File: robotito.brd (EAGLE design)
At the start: 76.2 x 85.1 mm, 44 parts, among them IC1 7805T, IC2 L298, IC3 L298

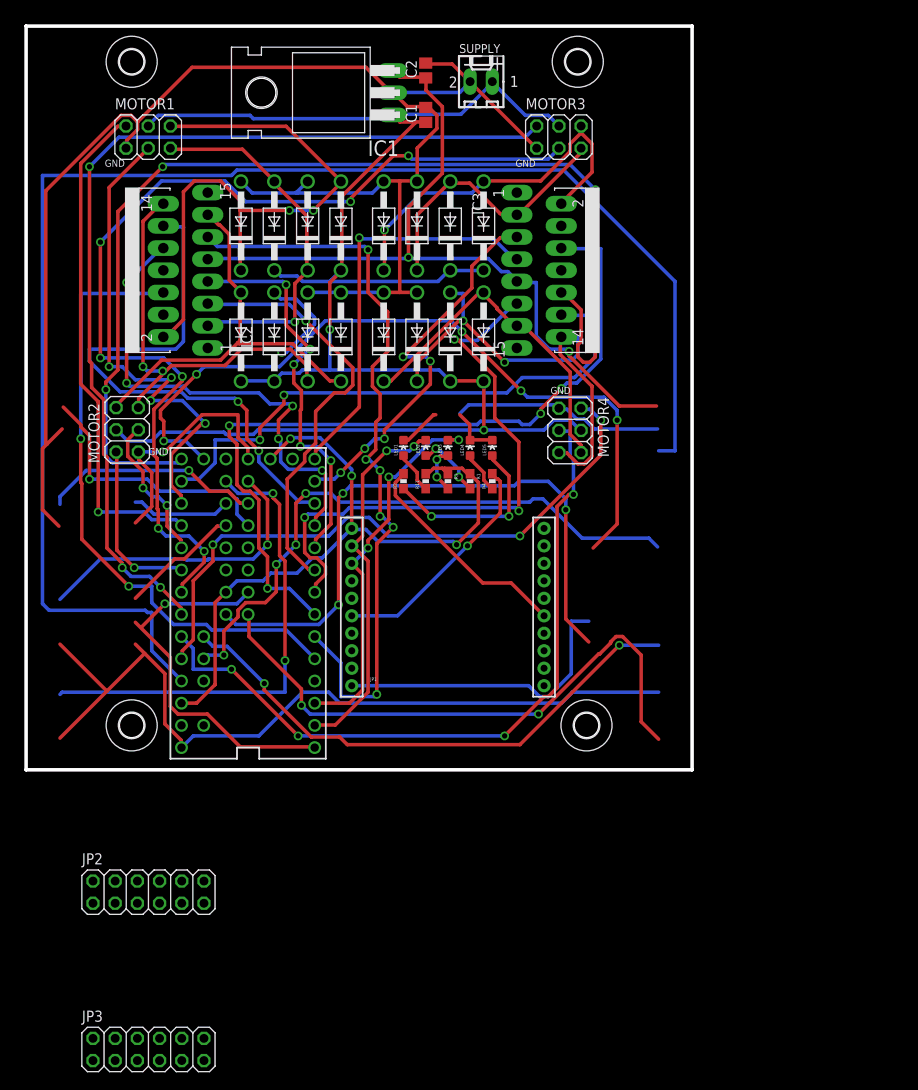
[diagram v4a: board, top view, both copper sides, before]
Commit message: switch to powerso and .1 inch for sensors
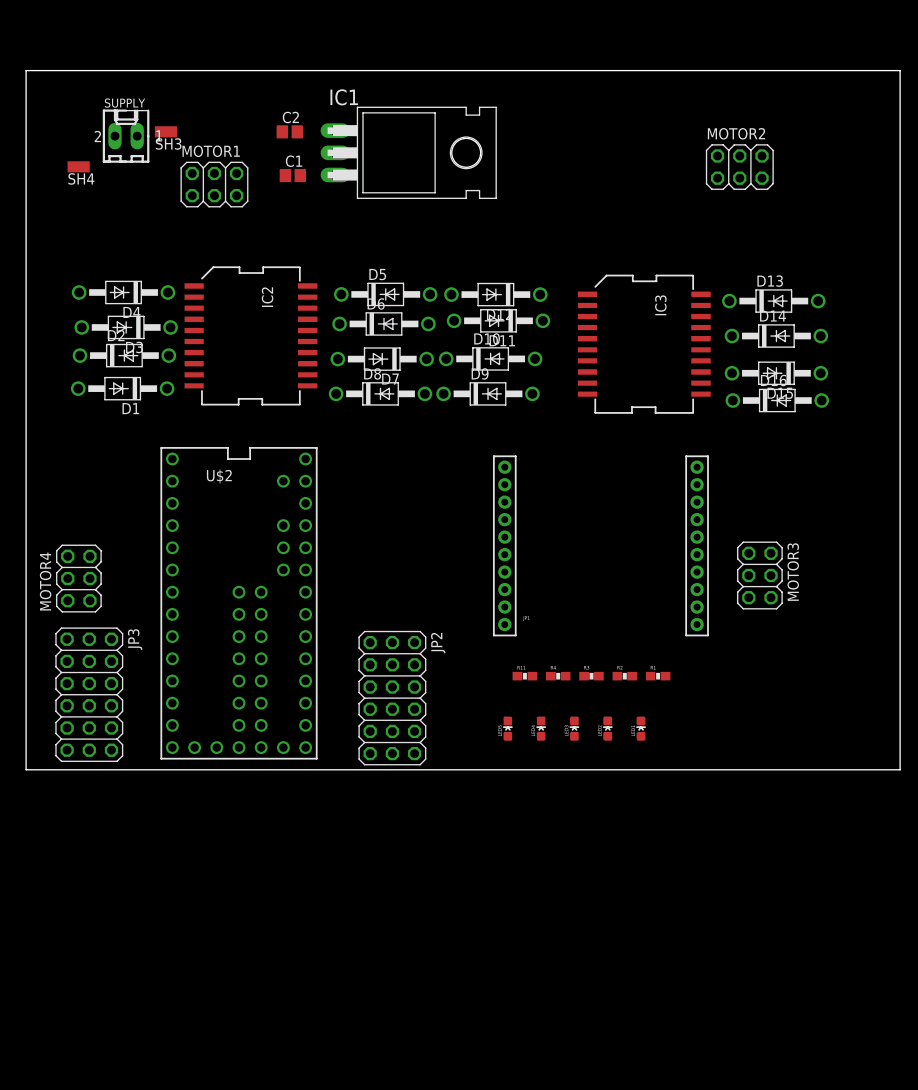
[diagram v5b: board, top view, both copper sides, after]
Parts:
- removed U$1, U$3, U$4, U$5: (no value), holes:2,8
- added SH3, SH4: SHORT-HT5, shorts-old:SHORT_TOP-50
- IC2, IC3: value L298 -> L298POWERSO-20; device st-microelectronics:MULTIWATT-15 -> mylibrary:POWERSO-20
- JP2, JP3: device pinhead:2X06 -> mylibrary:2X06
- moved MOTOR2 76.3 mm to (81.7, 69.0), turned to 0 degrees
- moved MOTOR4 58.7 mm to (6.04, 21.9), turned to 90 degrees
- moved MOTOR3 55.2 mm to (84.0, 22.2), turned to 270 degrees
- moved D16 45.6 mm to (86.0, 42.2), turned to 0 degrees
- moved LED1 42.1 mm to (70.4, 4.71)
- moved D15 41.3 mm to (85.8, 45.4), turned to 180 degrees
- moved SUPPLY 41.1 mm to (11.4, 72.5)
- moved JP3 41.0 mm to (8.50, 8.59), turned to 270 degrees
- moved LED2 38.3 mm to (66.5, 4.71)
- moved D14 37.3 mm to (85.8, 49.6), turned to 0 degrees
- moved JP2 36.7 mm to (43.2, 8.20), turned to 270 degrees
- moved LED3 35.2 mm to (62.7, 4.71)
- moved R2 33.7 mm to (68.5, 10.7), turned to 0 degrees
- moved D13 33.5 mm to (85.5, 53.6), turned to 0 degrees
- moved LED4 33.1 mm to (58.9, 4.71)
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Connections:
- removed net HB1GND: IC2.8
- removed net HB2GND: IC3.8
- new net LPGND: C1.2, C2.2, IC1.2, JP2.P11, JP2.P14, JP2.P17, JP2.P2, JP2.P5, JP2.P8, JP3.P11, JP3.P14, JP3.P17, JP3.P2, JP3.P5, JP3.P8, MOTOR1.1, MOTOR2.1, MOTOR3.1, MOTOR4.1, SH4.2, U$2.GND, U$2.GND1, U$2.GND2
- new net LPVCC: C1.1, IC1.1, MOTOR1.4, MOTOR2.4, MOTOR3.4, MOTOR4.4, SH3.2
- net +5V: now also IC2.12, IC3.12, JP2.P12, JP2.P15, JP2.P18, JP2.P3, JP2.P6, JP2.P9, JP3.P12, JP3.P15, JP3.P18, JP3.P3, JP3.P6, JP3.P9; no longer IC2.9, IC3.9
- net DS1: now also JP2.P1
- net DS10: now also JP3.P10
- net DS11: now also JP3.P13
- net DS12: now also JP3.P16
- net DS2: now also JP2.P4
- net DS3: now also JP2.P7
- net DS4: now also JP2.P10
- net DS5: now also JP2.P13
- net DS6: now also JP2.P16
- net DS7: now also JP3.P1
- net DS8: now also JP3.P4
- net DS9: now also JP3.P7
- net GND: now also IC2.10, IC2.11, IC2.19, IC2.2, IC2.20, IC3.10, IC3.11, IC3.19, IC3.2, IC3.20, SH4.1; no longer C1.2, C2.2, IC1.2, IC2.15, IC3.15, MOTOR1.1, MOTOR2.1, MOTOR3.1, MOTOR4.1, U$2.GND, U$2.GND1, U$2.GND2
- net M1EN: now also IC2.8; no longer IC2.6
- net M1I1: now also IC2.7; no longer IC2.5
- net M1I2: now also IC2.9; no longer IC2.7
- net M1M1: now also IC2.4; no longer IC2.2
- net M1M2: now also IC2.5; no longer IC2.3
- net M2EN: now also IC2.14; no longer IC2.11
- net M2I1: now also IC2.13; no longer IC2.10
- net M2I2: now also IC2.15; no longer IC2.12
- net M2M1: now also IC2.16; no longer IC2.13
- net M2M2: now also IC2.17; no longer IC2.14
- net M3EN: now also IC3.8; no longer IC3.6
- net M3I1: now also IC3.7; no longer IC3.5
- net M3I2: now also IC3.9; no longer IC3.7
- net M3M1: now also IC3.4; no longer IC3.2
- net M3M2: now also IC3.5; no longer IC3.3
- net M4EN: now also IC3.14; no longer IC3.11
- net M4I1: now also IC3.13; no longer IC3.10
- net M4I2: now also IC3.15; no longer IC3.12
- net M4M1: now also IC3.16; no longer IC3.13
- net M4M2: now also IC3.17; no longer IC3.14
- net VCC: now also IC2.6, IC3.6, SH3.1; no longer C1.1, IC1.1, IC2.4, IC3.4, MOTOR1.4, MOTOR2.4, MOTOR3.4, MOTOR4.4
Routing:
- net GND: track 323.3 -> 0.00 mm, vias 2 -> 0
- net VCC: track 204.9 -> 0.00 mm, vias 2 -> 0
- net +5V: track 183.1 -> 0.00 mm, vias 2 -> 0
- net DS1: track 170.3 -> 0.00 mm
- net M4I1: track 126.1 -> 0.00 mm, vias 3 -> 0
- net M3ENCA: track 114.0 -> 0.00 mm, vias 7 -> 0
- net M3ENCB: track 109.9 -> 0.00 mm, vias 3 -> 0
- net M3EN: track 91.0 -> 0.00 mm, vias 4 -> 0
- net M2EN: track 87.3 -> 0.00 mm, vias 6 -> 0
- net DS6: track 86.7 -> 0.00 mm, vias 5 -> 0
- net M4ENCA: track 83.3 -> 0.00 mm, vias 4 -> 0
- net +3.3V: track 80.6 -> 0.00 mm, vias 3 -> 0
- net M4ENCB: track 71.8 -> 0.00 mm, vias 3 -> 0
- net DS5: track 71.6 -> 0.00 mm, vias 3 -> 0
- net M1EN: track 71.1 -> 0.00 mm, vias 2 -> 0
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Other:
- board size 76.2 x 85.1 mm -> 100 x 80 mm
- board text removed: "+"
- board text removed: "-"
- board text removed: "GND"

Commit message: added pads to board
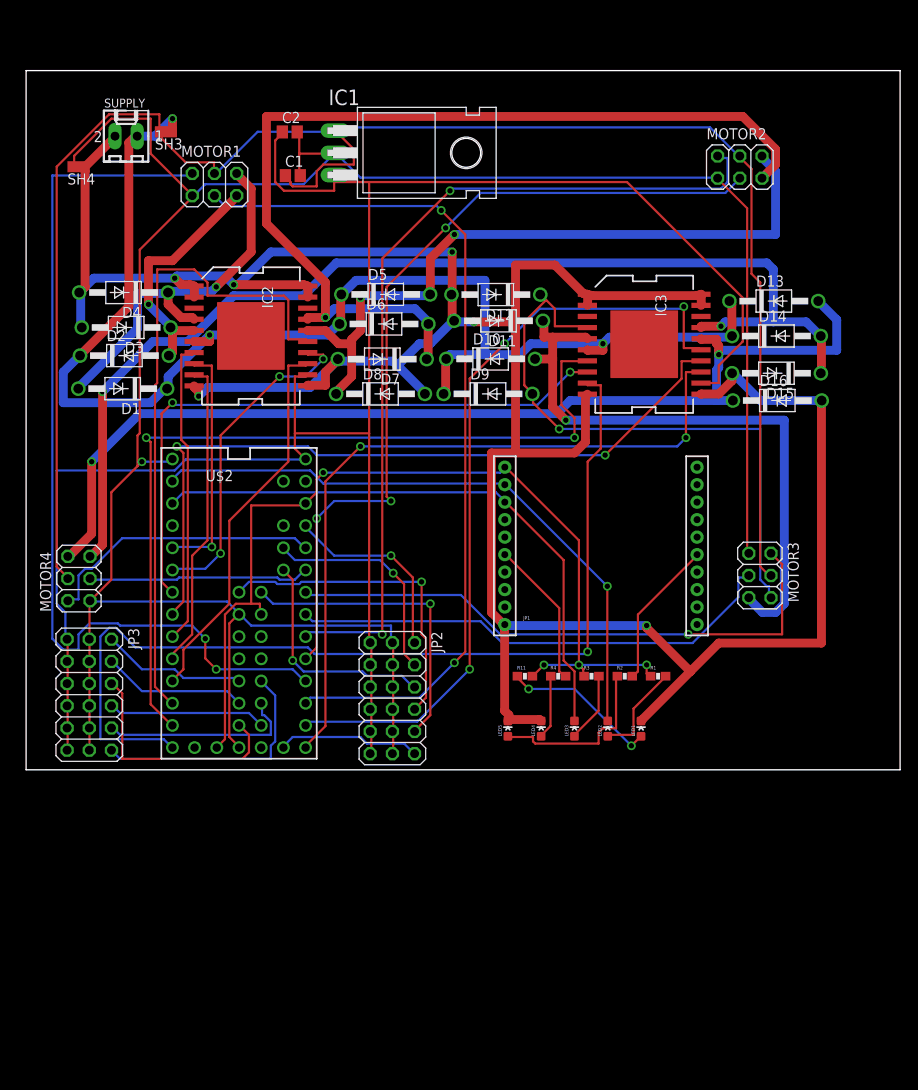
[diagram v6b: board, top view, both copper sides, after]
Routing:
- net GND: track 0.00 -> 334.3 mm, vias 0 -> 6
- net LPGND: track 0.00 -> 279.3 mm, vias 0 -> 1
- net +5V: track 0.00 -> 228.9 mm
- net LPVCC: track 0.00 -> 201.9 mm
- net VCC: track 0.00 -> 152.9 mm, vias 0 -> 3
- net M4M2: track 0.00 -> 127.6 mm, vias 0 -> 2
- net M4M1: track 0.00 -> 117.8 mm, vias 0 -> 2
- net M3I2: track 0.00 -> 110.8 mm, vias 0 -> 1
- net M2M2: track 0.00 -> 109.0 mm, vias 0 -> 1
- net +3.3V: track 0.00 -> 107.3 mm, vias 0 -> 4
- net M1ENCB: track 0.00 -> 105.0 mm, vias 0 -> 2
- net M2ENCB: track 0.00 -> 99.2 mm, vias 0 -> 2
- net M1ENCA: track 0.00 -> 99.0 mm, vias 0 -> 2
- net M2ENCA: track 0.00 -> 96.2 mm, vias 0 -> 3
- net M3I1: track 0.00 -> 95.5 mm, vias 0 -> 2
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
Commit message: added holes and resized
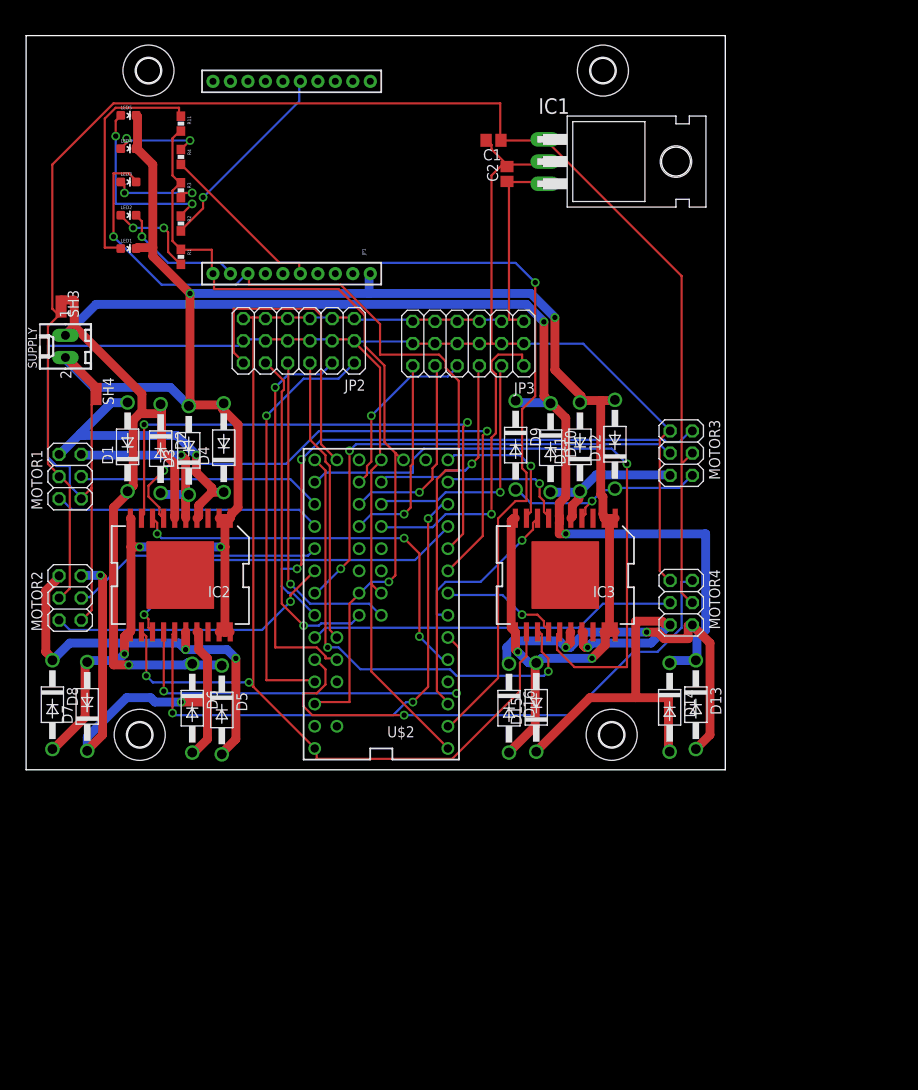
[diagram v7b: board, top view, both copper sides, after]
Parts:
- added U$1, U$3, U$4, U$5: (no value), holes:2,8
- moved MOTOR2 91.1 mm to (5.04, 19.7), turned to 90 degrees
- moved LED5 82.5 mm to (11.7, 74.9), turned to 270 degrees
- moved LED4 81.4 mm to (11.7, 71.1), turned to 270 degrees
- moved LED3 80.7 mm to (11.7, 67.3), turned to 270 degrees
- moved LED2 80.4 mm to (11.7, 63.5), turned to 270 degrees
- moved LED1 80.4 mm to (11.7, 59.6), turned to 270 degrees
- moved R11 74.5 mm to (17.7, 73.9), turned to 270 degrees
- moved R4 73.4 mm to (17.7, 70.1), turned to 270 degrees
- moved R3 72.8 mm to (17.7, 66.3), turned to 270 degrees
- moved R1 72.7 mm to (17.7, 58.7), turned to 270 degrees
- moved R2 72.5 mm to (17.7, 62.5), turned to 270 degrees
- moved MOTOR4 69.0 mm to (75.0, 19.1), turned to 270 degrees
- moved JP1 58.5 mm to (41.4, 67.8), turned to 90 degrees
- moved JP3 57.3 mm to (50.6, 47.5), turned to 180 degrees
- moved D7 52.1 mm to (6.99, 7.25), turned to 90 degrees
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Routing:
- net M3I2: track 110.8 -> 16.4 mm
- net M3I1: track 95.5 -> 15.2 mm, vias 2 -> 1
- net M4M2: track 127.6 -> 49.5 mm, vias 2 -> 1
- net M1ENCB: track 105.0 -> 30.6 mm, vias 2 -> 0
- net M4M1: track 117.8 -> 44.3 mm
- net M4EN: track 86.1 -> 13.7 mm, vias 2 -> 1
- net M1ENCA: track 99.0 -> 28.1 mm, vias 2 -> 0
- net +5V: track 228.9 -> 159.2 mm, vias 0 -> 2
- net GND: track 334.3 -> 266.4 mm, vias 6 -> 7
- net M2ENCA: track 96.2 -> 29.0 mm, vias 3 -> 0
- net M2ENCB: track 99.2 -> 32.9 mm, vias 2 -> 1
- net M2M2: track 109.0 -> 55.7 mm, vias 1 -> 2
- net LPGND: track 279.3 -> 226.8 mm, vias 1 -> 0
- net M3EN: track 71.9 -> 19.5 mm, vias 2 -> 1
- net M3M2: track 70.3 -> 18.0 mm, vias 1 -> 0
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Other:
- board size 100 x 80 mm -> 80 x 84 mm
- board text added: "5V"
- board text added: "GND"
- board text added: "Signal"

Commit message: fix routing errors. v .1
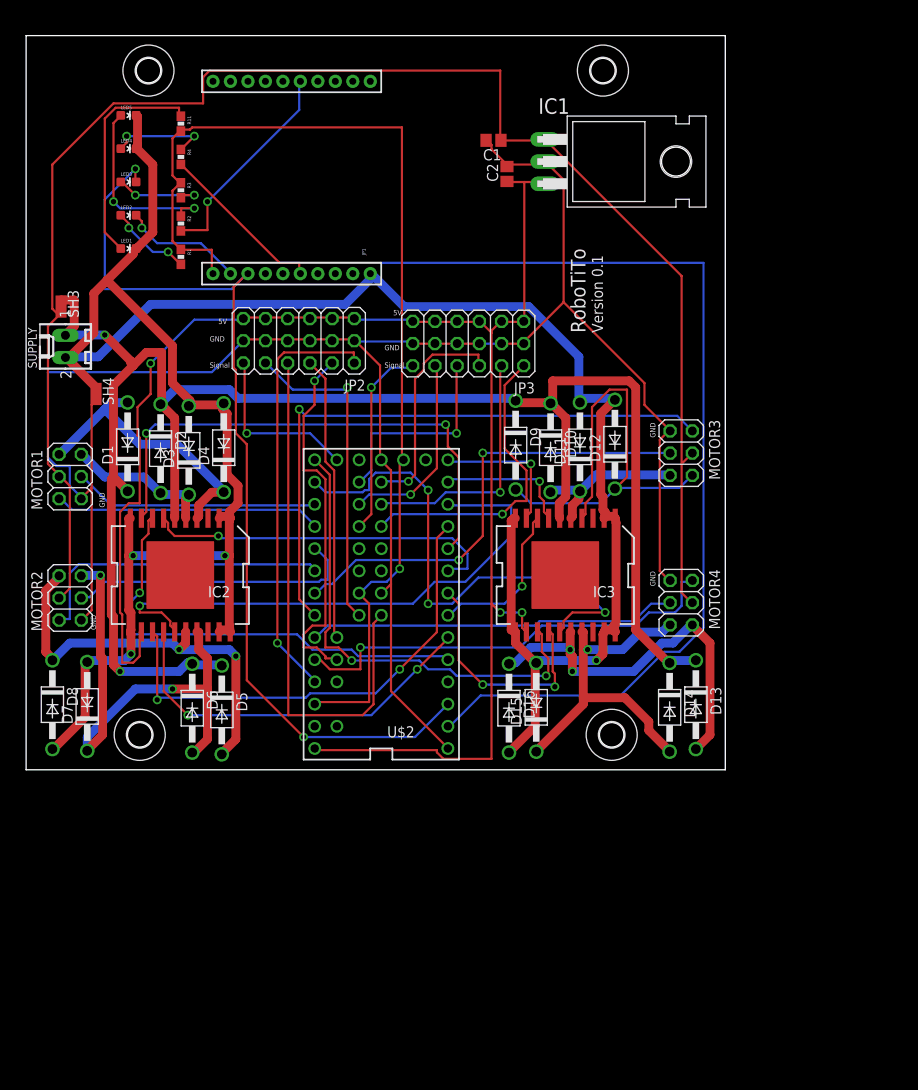
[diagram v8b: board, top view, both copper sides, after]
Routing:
- net RX: track 107.7 -> 145.0 mm, vias 2 -> 1
- net M3M1: track 24.6 -> 52.1 mm, vias 1 -> 0
- net +3.3V: track 96.3 -> 123.0 mm
- net +5V: track 159.2 -> 185.3 mm, vias 2 -> 3
- net DS4: track 37.3 -> 61.1 mm, vias 1 -> 0
- net M1I1: track 63.6 -> 41.0 mm, vias 2 -> 1
- net GND: track 266.4 -> 283.2 mm, vias 7 -> 4
- net M4I2: track 73.1 -> 58.7 mm, vias 1 -> 3
- net M2I1: track 41.4 -> 55.8 mm, vias 1 -> 2
- net DS6: track 34.2 -> 19.8 mm, vias 0 -> 1
- net M4EN: track 13.7 -> 27.2 mm, vias 1 -> 2
- net M4ENCB: track 62.2 -> 50.9 mm
- net M4M2: track 49.5 -> 40.2 mm
- net TX: track 100.3 -> 109.0 mm, vias 1 -> 2
- net LPVCC: track 178.3 -> 185.3 mm
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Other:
- board text added: "RoboTiTo"
- board text added: "Version 0.1"
